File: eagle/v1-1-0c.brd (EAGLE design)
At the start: 313 x 132.9 mm, 179 parts, among them J1 CR22A-44D-2.54DSA(70), J3 26-60-4040, J4 AUDIO_JACK_3.5MM_PTH, J5 DIN5, SW1 3PDT-AQ-SWITCH, SW2 9077-1, U10 7805, U11 74LS10N, U13 74LS04N, U14 4528N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

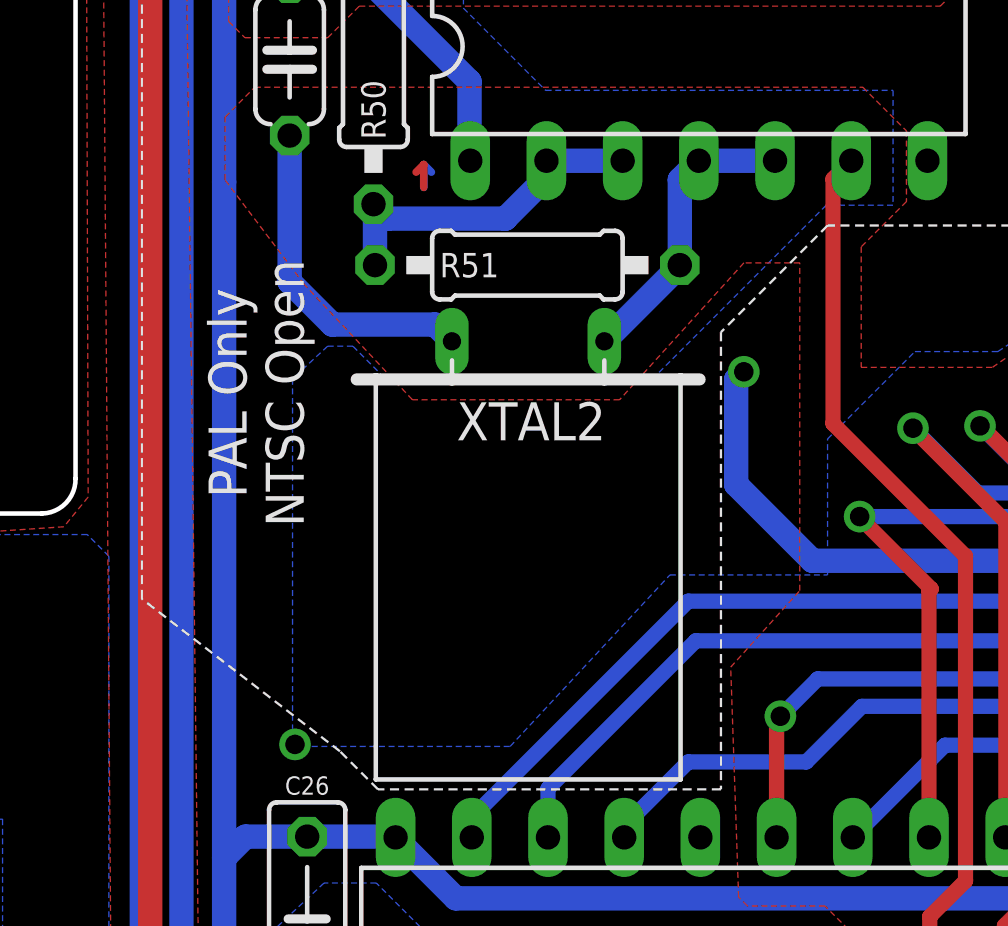
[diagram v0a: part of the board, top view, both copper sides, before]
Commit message: XTAL Boost cap added
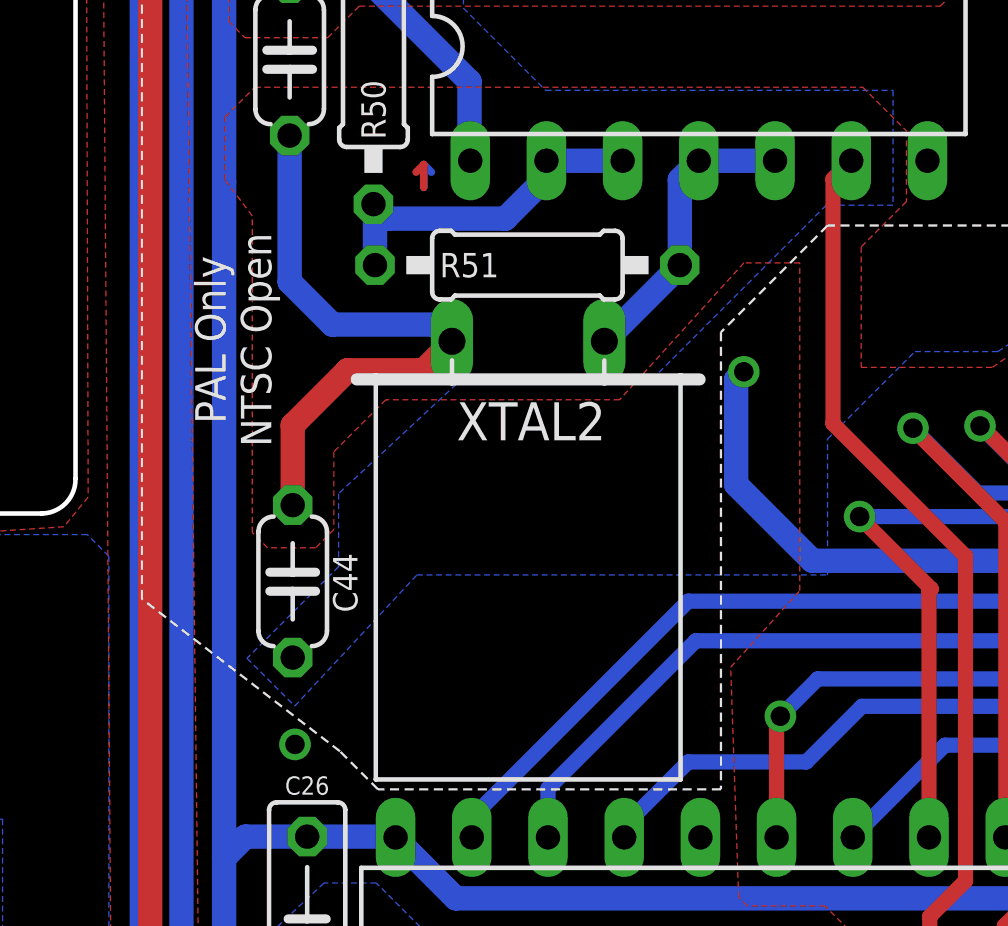
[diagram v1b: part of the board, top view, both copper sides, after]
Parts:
- added C44: ∞/22pF, aq-rcl:C050-024X044
- XTAL2: device special:Q -> aq-special:Q
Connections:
- net GND: now also C44.2
- net N$208: now also C44.1
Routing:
- net N$208: track 11.1 -> 20.3 mm
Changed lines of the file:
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@@
 <wire x1="25.654" y1="50.546" x2="14.224" y2="50.546" width="0.0762" layer="21" style="shortdash"/>
 <wire x1="14.224" y1="50.546" x2="12.954" y2="51.816" width="0.0762" layer="21" style="shortdash"/>
-<text x="10.16" y="63.754" size="1.27" layer="21" rot="R90" align="center">PAL Only
+<text x="9.398" y="65.532" size="1.016" layer="21" rot="R90" align="center">PAL Only
 NTSC Open</text>
 <text x="202.9714" y="98.2218" size="1.27" layer="21" align="center">NTSC Only</text>
@@
 <attribute name="VALUE" x="21.844" y="68.0466" size="0.8128" layer="27" ratio="10" align="center-right"/>
 </element>
-<element name="XTAL2" library="special" library_urn="urn:adsk.eagle:library:367" package="Q" package3d_urn="urn:adsk.eagle:package:26649/1" value="∞/7.15909 Mhz" x="19.2278" y="57.8612" smashed="yes" rot="R180">
+<element name="XTAL2" library="aq-special" package="Q" package3d_urn="urn:adsk.eagle:package:26649/1" value="∞/7.15909 Mhz" x="19.2278" y="57.8612" smashed="yes" rot="R180">
 <attribute name="NAME" x="19.3294" y="62.8142" size="1.27" layer="25" ratio="10" rot="R180" align="center"/>
 <attribute name="POPULARITY" value="12" x="19.2278" y="57.8612" size="1.778" layer="27" rot="R180" display="off"/>
@@
 <attribute name="VALUE" x="109.728" y="9.779" size="1.27" layer="27"/>
 </element>
+<element name="C44" library="aq-rcl" package="C050-024X044" package3d_urn="urn:adsk.eagle:package:23643/1" value="∞/22pF" x="11.3792" y="57.4802" smashed="yes" rot="R270">
+<attribute name="NAME" x="12.7254" y="58.42" size="0.8128" layer="25" ratio="10" rot="R270"/>
+<attribute name="POPULARITY" value="14" x="11.3792" y="57.4802" size="1.778" layer="27" rot="R270" display="off"/>
+<attribute name="SPICEPREFIX" value="C" x="11.3792" y="57.4802" size="1.778" layer="27" rot="R270" display="off"/>
+<attribute name="VALUE" x="8.9662" y="59.5376" size="0.8128" layer="27" ratio="10" rot="R270"/>
+</element>
 </elements>
 <signals>
@@
 <vertex x="26.41888125" y="68.096259375"/>
 <vertex x="22.27561875" y="63.53266875"/>
-<vertex x="15.37018125" y="63.53266875"/>
-<vertex x="11.76735" y="67.375690625"/>
+<vertex x="14.48526875" y="63.53266875"/>
+<vertex x="12.7508" y="61.7982"/>
+<vertex x="12.7508" y="59.2074"/>
+<vertex x="12.1412" y="58.5978"/>
+<vertex x="10.541" y="58.5978"/>
+<vertex x="10.033" y="59.1058"/>
+<vertex x="10.033" y="69.661878125"/>
 <vertex x="9.12526875" y="70.85843125"/>
 <vertex x="9.12526875" y="72.960090625"/>
@@
 </polygon>
 <polygon width="0.025" layer="16">
-<vertex x="11.373340625" y="64.23185625"/>
-<vertex x="11.373340625" y="51.977109375"/>
-<vertex x="18.626959375" y="51.977109375"/>
-<vertex x="23.9532" y="57.69308125"/>
+<vertex x="12.908503125" y="60.406315625"/>
+<vertex x="12.908503125" y="57.968103125"/>
+<vertex x="9.8552" y="54.9148"/>
+<vertex x="11.44706875" y="53.32293125"/>
+<vertex x="15.51924375" y="57.69308125"/>
 <vertex x="29.207340625" y="57.69308125"/>
 <vertex x="29.207340625" y="62.226640625"/>
@@
 <vertex x="29.162290625" y="70.01778125"/>
 <vertex x="23.41276875" y="64.268240625"/>
-<vertex x="14.435690625" y="64.268240625"/>
-<vertex x="13.38488125" y="65.31908125"/>
-<vertex x="12.544209375" y="65.31908125"/>
+<vertex x="17.06754375" y="64.268240625"/>
 </polygon>
 <polygon width="0.025" layer="16">
@@
 <wire x1="27.6352" y1="19.7612" x2="27.6352" y2="24.384" width="0.8128" layer="16"/>
 <wire x1="27.6352" y1="24.384" x2="27.686" y2="24.4348" width="0.8128" layer="16"/>
+<contactref element="C44" pad="2"/>
 <wire x1="185.1152" y1="58.4708" x2="190.0682" y2="73.9394" width="0" layer="19" extent="1-1"/>
 </signal>
@@
 <wire x1="16.6878" y1="65.4812" x2="16.129" y2="66.04" width="0.8128" layer="16"/>
 <wire x1="16.129" y1="66.04" x2="12.7" y2="66.04" width="0.8128" layer="16"/>
+<contactref element="C44" pad="1"/>
+<wire x1="11.3792" y1="60.0202" x2="11.3792" y2="62.6872" width="0.8128" layer="1"/>
+<wire x1="13.208" y1="64.516" x2="15.748" y2="64.516" width="0.8128" layer="1"/>
+<wire x1="15.748" y1="64.516" x2="16.6878" y2="65.4558" width="0.8128" layer="1"/>
+<wire x1="16.6878" y1="65.4558" x2="16.6878" y2="65.4812" width="0.8128" layer="1"/>
+<wire x1="11.3792" y1="62.6872" x2="13.208" y2="64.516" width="0.8128" layer="1"/>
 </signal>
 <signal name="N$223">

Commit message: 09 DEC Update
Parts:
- removed TR1: (no value), aq-rcl:10MM-DUAL
- added L-V1: 10uH @ 4.43MHz, aq-rcl:10MM-VAR-IND
- C32: value 100pF -> 100pF/47pF
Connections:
- net GND: no longer TR1.P$3, TR1.P$4
- net N$691: now also L-V1.P$1, L-V1.P$3; no longer TR1.P$2
- net VPP: now also L-V1.P$2, L-V1.P$4; no longer TR1.P$1
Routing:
- net VPP: track 511.1 -> 510.4 mm
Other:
- board text added: "Aquarius Motherboard v1.1.0 Rev C - 09 DEC 2020 by Sean Harrington, sph@1stage.com"
- board text added: "Optional Chroma Timing"
- board text removed: "Aquarius Motherboard v1.1.0 Rev C - 21 OCT 2020 by Sean Harrington, sph@1stage.com"
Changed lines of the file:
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@@
 <text x="108.966" y="114.3" size="1.778" layer="21" align="center">RF Modulator</text>
 <text x="266.7" y="54.102" size="1.778" layer="21" align="center">Aquarius Motherboard v1.1.0
-Rev C - 21 OCT 2020
+Rev C - 09 DEC 2020
 by Sean Harrington, sph@1stage.com</text>
 <text x="44.2976" y="8.3058" size="0.8128" layer="21" rot="R180" align="center">This replaces
@@
 NTSC-2Φ</text>
 <wire x1="111.9378" y1="7.9502" x2="111.0234" y2="10.3886" width="0.1524" layer="21"/>
+<wire x1="212.9282" y1="94.2594" x2="230.3526" y2="94.3356" width="0.1524" layer="21" style="shortdash"/>
+<wire x1="230.3526" y1="94.3356" x2="230.3018" y2="106.426" width="0.1524" layer="21" style="shortdash"/>
+<wire x1="230.3018" y1="106.426" x2="230.3018" y2="107.1372" width="0.1524" layer="21" style="shortdash"/>
+<wire x1="230.3018" y1="107.1372" x2="219.6592" y2="107.2388" width="0.1524" layer="21" style="shortdash"/>
+<wire x1="219.6592" y1="107.2388" x2="219.3036" y2="105.0544" width="0.1524" layer="21" style="shortdash"/>
+<wire x1="219.3036" y1="105.0544" x2="219.202" y2="101.9556" width="0.1524" layer="21" style="shortdash"/>
+<wire x1="219.202" y1="101.9556" x2="215.5952" y2="101.981" width="0.1524" layer="21" style="shortdash"/>
+<wire x1="215.5952" y1="101.981" x2="215.6206" y2="95.7834" width="0.1524" layer="21" style="shortdash"/>
+<wire x1="215.6206" y1="95.7834" x2="212.8266" y2="95.7834" width="0.1524" layer="21" style="shortdash"/>
+<wire x1="212.8266" y1="95.7834" x2="212.852" y2="94.2848" width="0.1524" layer="21" style="shortdash"/>
+<text x="231.3178" y="100.5332" size="0.8128" layer="21" rot="R90" align="center">Optional Chroma Timing</text>
 </plain>
 <attributes>
@@
 <attribute name="VALUE" x="165.862" y="101.4222" size="0.6096" layer="27" ratio="10" align="top-center"/>
 </element>
-<element name="C32" library="aq-rcl" package="C025-024X044" package3d_urn="urn:adsk.eagle:package:23630/1" value="100pF" x="217.0684" y="98.8568" smashed="yes" rot="R90">
+<element name="C32" library="aq-rcl" package="C025-024X044" package3d_urn="urn:adsk.eagle:package:23630/1" value="100pF/47pF" x="217.0684" y="98.8568" smashed="yes" rot="R90">
 <attribute name="NAME" x="216.0016" y="101.3206" size="0.8128" layer="25" ratio="10"/>
 <attribute name="POPULARITY" value="17" x="217.0684" y="98.8568" size="1.778" layer="27" rot="R90" display="off"/>
 <attribute name="SPICEPREFIX" value="C" x="217.0684" y="98.8568" size="1.778" layer="27" rot="R90" display="off"/>
-<attribute name="VALUE" x="218.5924" y="96.4438" size="0.8128" layer="27" ratio="10" rot="R180"/>
+<attribute name="VALUE" x="219.3544" y="95.4278" size="0.8128" layer="27" ratio="10" rot="R180"/>
 </element>
 <element name="C14" library="aq-rcl" package="C050-024X044" package3d_urn="urn:adsk.eagle:package:23643/1" value=".022uF" x="214.1982" y="99.4156" smashed="yes" rot="R90">
@@
 <attribute name="SF_ID" value="PRT-08032" x="194.5132" y="127.9906" size="1.778" layer="27" rot="R270" display="off"/>
 </element>
-<element name="TR1" library="aq-rcl" package="10MM-DUAL" value="" x="224.0026" y="100.2792" smashed="yes">
-<attribute name="NAME" x="227.1268" y="94.3356" size="1.27" layer="21" align="bottom-center"/>
-<attribute name="VALUE" x="223.3676" y="96.0882" size="1.27" layer="21" align="top-center"/>
-</element>
 <element name="C38" library="aq-rcl" package="C050-025X085" value="100pF" x="45.9486" y="15.9004" smashed="yes" rot="R90">
 <attribute name="NAME" x="45.9994" y="20.4216" size="0.6096" layer="25" ratio="10" align="bottom-center"/>
@@
 <attribute name="VALUE" x="8.9662" y="59.5376" size="0.8128" layer="27" ratio="10" rot="R270"/>
 </element>
+<element name="L-V1" library="aq-rcl" package="10MM-VAR-IND" value="10uH @ 4.43MHz" x="223.901" y="100.2792" smashed="yes">
+<attribute name="NAME" x="221.361" y="106.3498" size="1.016" layer="25" align="center"/>
+<attribute name="VALUE" x="229.362" y="100.2792" size="1.016" layer="27" rot="R90" align="center"/>
+</element>
 </elements>
 <signals>
@@
 <contactref element="J4" pad="SLEEVE"/>
 <contactref element="Q1" pad="3"/>
-<contactref element="TR1" pad="P$4"/>
-<contactref element="TR1" pad="P$3"/>
 <contactref element="R30" pad="1"/>
 <contactref element="C38" pad="1"/>
@@
 <wire x1="216.9922" y1="126.528284375" x2="216.8652" y2="126.401284375" width="0.8128" layer="1"/>
 <wire x1="216.8652" y1="126.401284375" x2="216.8652" y2="124.714" width="0.8128" layer="1"/>
-<contactref element="C32" pad="1"/>
-<wire x1="217.0684" y1="97.5868" x2="216.789" y2="97.5868" width="0.8128" layer="16"/>
 <wire x1="216.789" y1="97.5868" x2="215.519" y2="98.8568" width="0.8128" layer="16"/>
 <wire x1="214.0204" y1="118.1608" x2="214.0204" y2="120.0404" width="0.8128" layer="1"/>
@@
 <wire x1="190.0682" y1="80.9244" x2="190.0682" y2="81.1022" width="0.8128" layer="1"/>
 <wire x1="190.0682" y1="81.1022" x2="192.1256" y2="83.1596" width="0.8128" layer="1"/>
-<contactref element="TR1" pad="P$1"/>
-<wire x1="217.0684" y1="97.5868" x2="219.71" y2="97.5868" width="0.8128" layer="16"/>
-<wire x1="219.71" y1="97.5868" x2="220.4466" y2="96.8502" width="0.8128" layer="16"/>
-<wire x1="220.4466" y1="96.8502" x2="220.8276" y2="96.4692" width="0.8128" layer="16"/>
 <wire x1="220.8276" y1="96.4692" x2="220.8276" y2="92.71" width="0.8128" layer="16"/>
 <wire x1="200.533" y1="77.978" x2="199.4154" y2="79.0956" width="0.8128" layer="1"/>
@@
 <wire x1="239.8014" y1="62.865" x2="242.0366" y2="62.865" width="0.8128" layer="16"/>
 <wire x1="242.0366" y1="62.865" x2="247.142" y2="67.9704" width="0.8128" layer="16"/>
+<contactref element="C32" pad="1"/>
+<contactref element="L-V1" pad="P$2"/>
+<contactref element="L-V1" pad="P$4"/>
+<wire x1="217.0684" y1="97.5868" x2="219.71" y2="97.5868" width="0.8128" layer="16"/>
+<wire x1="220.345" y1="96.9518" x2="219.71" y2="97.5868" width="0.8128" layer="16"/>
+<wire x1="220.345" y1="96.7232" x2="220.345" y2="96.9518" width="0.8128" layer="16"/>
+<wire x1="220.8276" y1="96.4692" x2="227.33" y2="96.7232" width="0" layer="19" extent="16-16"/>
+<wire x1="220.345" y1="96.7232" x2="220.8276" y2="96.4692" width="0" layer="19" extent="16-16"/>
+<wire x1="216.789" y1="97.5868" x2="217.0684" y2="97.5868" width="0" layer="19" extent="16-16"/>
 </signal>
 <signal name="N$105">
@@
 <contactref element="C32" pad="2"/>
 <contactref element="C14" pad="2"/>
-<contactref element="TR1" pad="P$2"/>
 <wire x1="214.1982" y1="101.9556" x2="215.2396" y2="101.9556" width="0.8128" layer="16"/>
 <wire x1="215.2396" y1="101.9556" x2="217.0684" y2="100.1268" width="0.8128" layer="16"/>
 <wire x1="217.0684" y1="100.1268" x2="217.0684" y2="100.457" width="0.8128" layer="16"/>
-<wire x1="217.0684" y1="100.457" x2="220.4466" y2="103.8352" width="0.8128" layer="16"/>
+<contactref element="L-V1" pad="P$1"/>
+<contactref element="L-V1" pad="P$3"/>
+<wire x1="217.0684" y1="100.1268" x2="220.345" y2="103.4034" width="0.8128" layer="16"/>
+<wire x1="220.345" y1="103.4034" x2="220.345" y2="103.8352" width="0.8128" layer="16"/>
+<wire x1="220.345" y1="103.8352" x2="227.33" y2="103.8352" width="0" layer="19" extent="1-1"/>
 </signal>
 <signal name="N$84">

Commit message: January fixes
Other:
- board text added: "Aquarius Motherboard v1.1.0 Rev C - 15 JAN 2021 by Sean Harrington, sph@1stage.com"
- board text removed: "Aquarius Motherboard v1.1.0 Rev C - 09 DEC 2020 by Sean Harrington, sph@1stage.com"
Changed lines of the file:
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@@
 <text x="108.966" y="114.3" size="1.778" layer="21" align="center">RF Modulator</text>
 <text x="266.7" y="54.102" size="1.778" layer="21" align="center">Aquarius Motherboard v1.1.0
-Rev C - 09 DEC 2020
+Rev C - 15 JAN 2021
 by Sean Harrington, sph@1stage.com</text>
 <text x="44.2976" y="8.3058" size="0.8128" layer="21" rot="R180" align="center">This replaces

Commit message: Rev C Full Release
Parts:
- C16: value 82pF/∞ -> ∞/82pF
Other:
- board text added: "Aquarius Motherboard v1.1.0 Rev C - 19 JAN 2021 by Sean Harrington, sph@1stage.com"
- board text added: "NTSC Passthrough"
- board text added: "PAL Only"
- board text removed: "Aquarius Motherboard v1.1.0 Rev C - 15 JAN 2021 by Sean Harrington, sph@1stage.com"
- board text removed: "PAL Only NTSC Passthrough"
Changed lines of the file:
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@@
 <wire x1="99.06" y1="82.042" x2="96.266" y2="84.836" width="0.0762" layer="21" style="shortdash"/>
 <wire x1="96.266" y1="84.836" x2="96.266" y2="89.662" width="0.0762" layer="21" style="shortdash"/>
-<text x="101.8032" y="94.0054" size="0.8128" layer="21" rot="R180" align="center">PAL Only
-NTSC Passthrough</text>
+<text x="101.8032" y="94.0054" size="0.8128" layer="21" rot="R180" align="center">PAL Only</text>
 <wire x1="20.828" y1="87.63" x2="18.034" y2="90.424" width="0.0762" layer="21" style="shortdash"/>
 <wire x1="18.034" y1="90.424" x2="18.034" y2="94.234" width="0.0762" layer="21" style="shortdash"/>
@@
 <wire x1="218.948" y1="107.95" x2="218.948" y2="104.394" width="0.0762" layer="21" style="shortdash"/>
 <wire x1="102.87" y1="91.44" x2="103.886" y2="91.44" width="0.0762" layer="21"/>
-<wire x1="103.886" y1="91.44" x2="105.41" y2="89.916" width="0.0762" layer="21"/>
-<wire x1="105.41" y1="89.916" x2="105.41" y2="84.836" width="0.0762" layer="21"/>
-<wire x1="105.41" y1="84.836" x2="104.394" y2="83.82" width="0.0762" layer="21"/>
+<wire x1="103.886" y1="91.44" x2="105.41" y2="89.916" width="0.1524" layer="21"/>
+<wire x1="105.41" y1="89.916" x2="105.41" y2="84.836" width="0.1524" layer="21"/>
+<wire x1="105.41" y1="84.836" x2="104.394" y2="83.82" width="0.1524" layer="21"/>
 <wire x1="104.394" y1="83.82" x2="103.124" y2="83.82" width="0.0762" layer="21"/>
 <text x="178.5874" y="106.6038" size="0.8128" layer="21" align="center">PAL Only U16-11 to Q6-2</text>
@@
 <text x="108.966" y="114.3" size="1.778" layer="21" align="center">RF Modulator</text>
 <text x="266.7" y="54.102" size="1.778" layer="21" align="center">Aquarius Motherboard v1.1.0
-Rev C - 15 JAN 2021
+Rev C - 19 JAN 2021
 by Sean Harrington, sph@1stage.com</text>
 <text x="44.2976" y="8.3058" size="0.8128" layer="21" rot="R180" align="center">This replaces
@@
 <wire x1="212.8266" y1="95.7834" x2="212.852" y2="94.2848" width="0.1524" layer="21" style="shortdash"/>
 <text x="231.3178" y="100.5332" size="0.8128" layer="21" rot="R90" align="center">Optional Chroma Timing</text>
+<text x="107.8738" y="86.3346" size="0.8128" layer="21" align="center-left">NTSC
+Passthrough</text>
+<wire x1="105.4608" y1="86.3854" x2="107.442" y2="86.3854" width="0.1524" layer="25"/>
 </plain>
 <attributes>
@@
 </element>
 <element name="L4" library="aq-rcl" package="TFI0305" package3d_urn="urn:adsk.eagle:package:23529/1" value="" x="102.8954" y="87.4776" smashed="yes" rot="R90">
-<attribute name="NAME" x="104.6226" y="88.1832" size="0.9906" layer="25" ratio="10"/>
+<attribute name="NAME" x="101.3008" y="86.868" size="0.9906" layer="25" ratio="10" rot="R90"/>
 <attribute name="POPULARITY" value="0" x="102.8954" y="87.4776" size="1.778" layer="27" rot="R90" display="off"/>
 <attribute name="SPICEPREFIX" value="L" x="102.8954" y="87.4776" size="1.778" layer="27" rot="R90" display="off"/>
@@
 <attribute name="VALUE" x="88.773" y="84.7852" size="0.8128" layer="27" ratio="10"/>
 </element>
-<element name="C16" library="aq-rcl" package="C050-024X044" package3d_urn="urn:adsk.eagle:package:23643/1" value="82pF/∞" x="98.6282" y="89.408" smashed="yes" rot="R270">
+<element name="C16" library="aq-rcl" package="C050-024X044" package3d_urn="urn:adsk.eagle:package:23643/1" value="∞/82pF" x="98.6282" y="89.408" smashed="yes" rot="R270">
 <attribute name="NAME" x="100.8126" y="90.2208" size="0.8128" layer="25" ratio="10" rot="R90"/>
 <attribute name="POPULARITY" value="14" x="98.6282" y="89.408" size="1.778" layer="27" rot="R270" display="off"/>
